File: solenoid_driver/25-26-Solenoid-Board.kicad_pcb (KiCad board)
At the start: 2 copper layers, 61.3 x 40.9 mm, 18 parts, among them J1 xt30, J2 JST-PH-K, J3 Screw_Terminal_01x08, U1 Teensy4.1, U2 LD1117S50TR_SOT223, U3 PTCAN3414DDFR, U4 ULN2308C

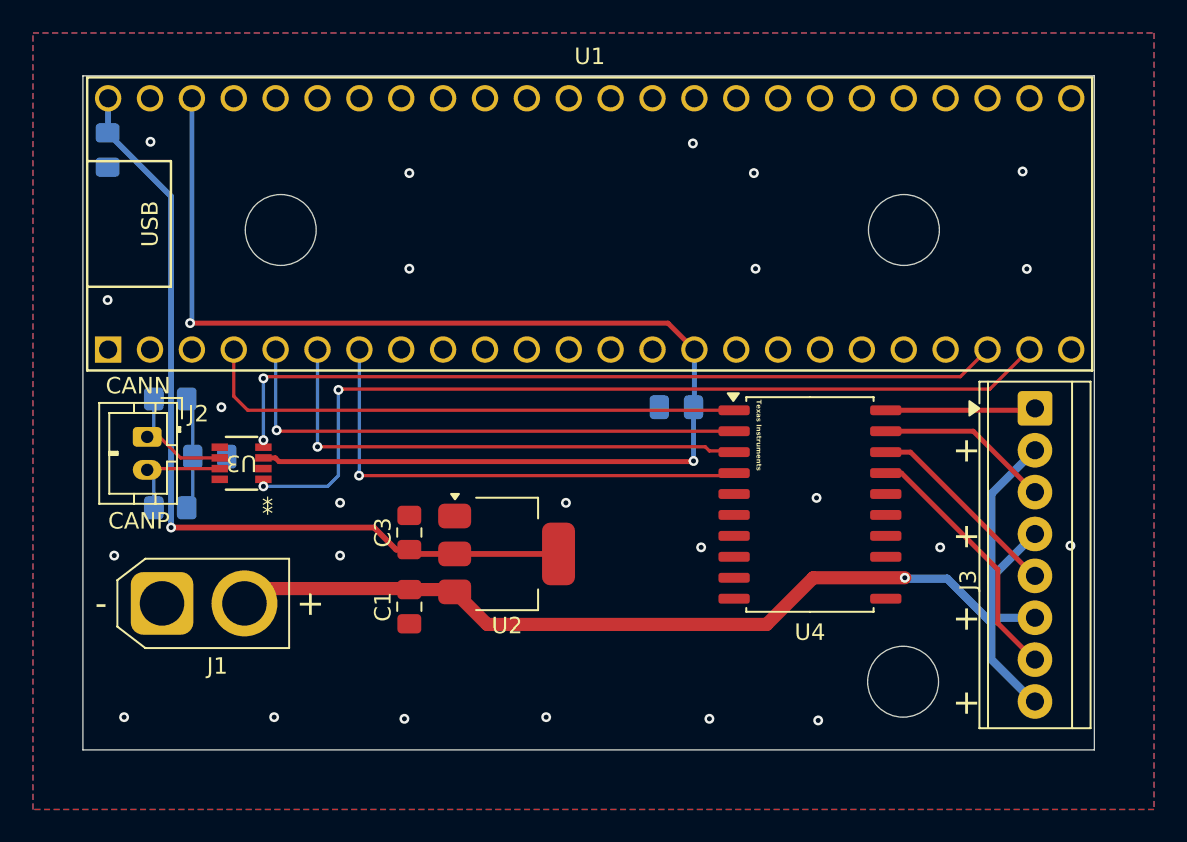
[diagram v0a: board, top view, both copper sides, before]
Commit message: Fixed what Sylvestor brought up
fixed tcan package, set 3d models, moved a few things around, and set supplementary circuits as do not populate.

did not add the mentioned diode
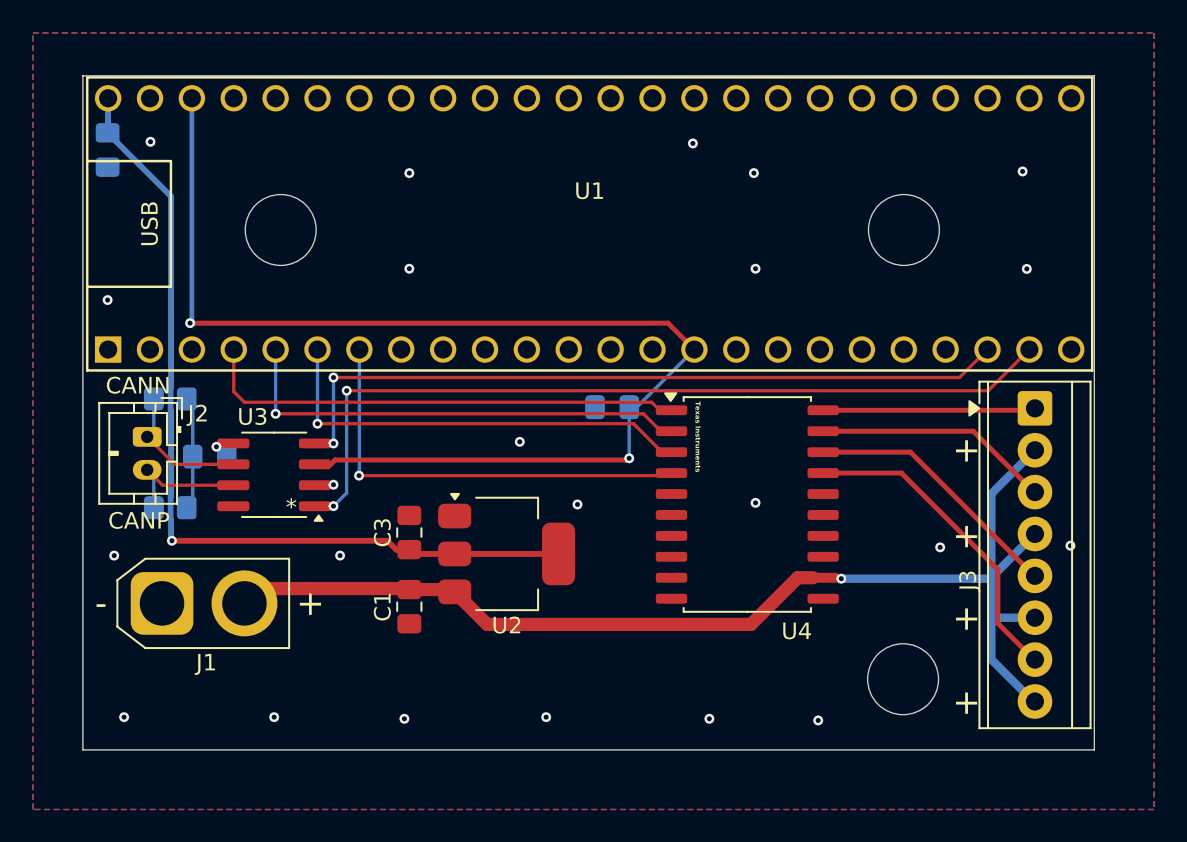
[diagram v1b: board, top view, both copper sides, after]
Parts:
- U3: value PTCAN3414DDFR -> PTCAN3414DR; footprint TCAN:SOT-23-THIN-8_DDF_TEX -> Package_SO:SOIC-8_3.9x4.9mm_P1.27mm
- moved G*** 5.82 mm to (91.5, 94.8)
- moved C4 3.90 mm to (96.1, 82.6)
- moved U4 3.80 mm to (104.3, 88.5)
- moved U3 2.10 mm to (75.6, 86.7)
- moved H1 0.15 mm to (113.8, 99.1)
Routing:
- net pin3: track 31.3 -> 26.0 mm
- net +3V3: track 77.9 -> 72.7 mm
- net pin2: track 32.7 -> 27.8 mm
- net pin1: track 33.5 -> 28.9 mm
- net pin4: track 30.5 -> 26.7 mm
- net S3: track 12.2 -> 16.0 mm
- net S2: track 10.6 -> 14.4 mm
- net S1: track 9.08 -> 12.9 mm
- net S4: track 15.7 -> 19.5 mm
- net C_RX: track 48.8 -> 45.5 mm
- net C_TX: track 53.4 -> 50.9 mm
- net CAN P: track 6.90 -> 8.08 mm
- net CAN N: track 7.39 -> 8.38 mm
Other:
- board text added: "*"
- board text removed: "DO NOT MOUNT"
